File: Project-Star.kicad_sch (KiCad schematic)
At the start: 0 parts

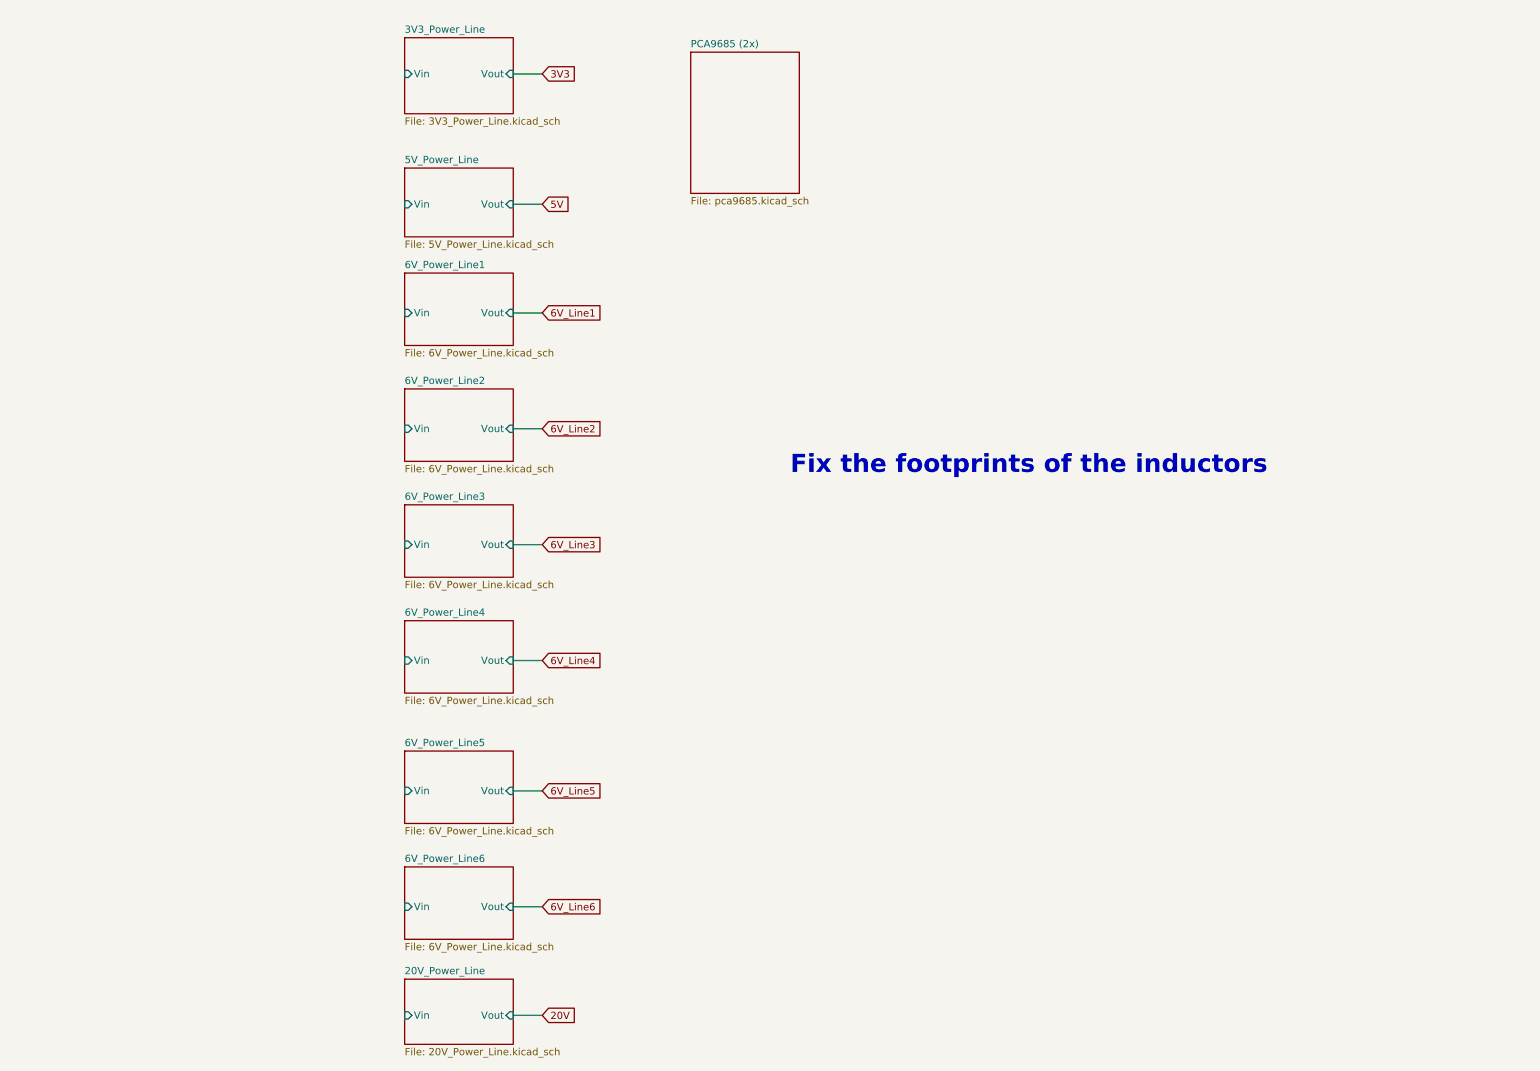
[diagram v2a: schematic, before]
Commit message: 20V line PCB v1
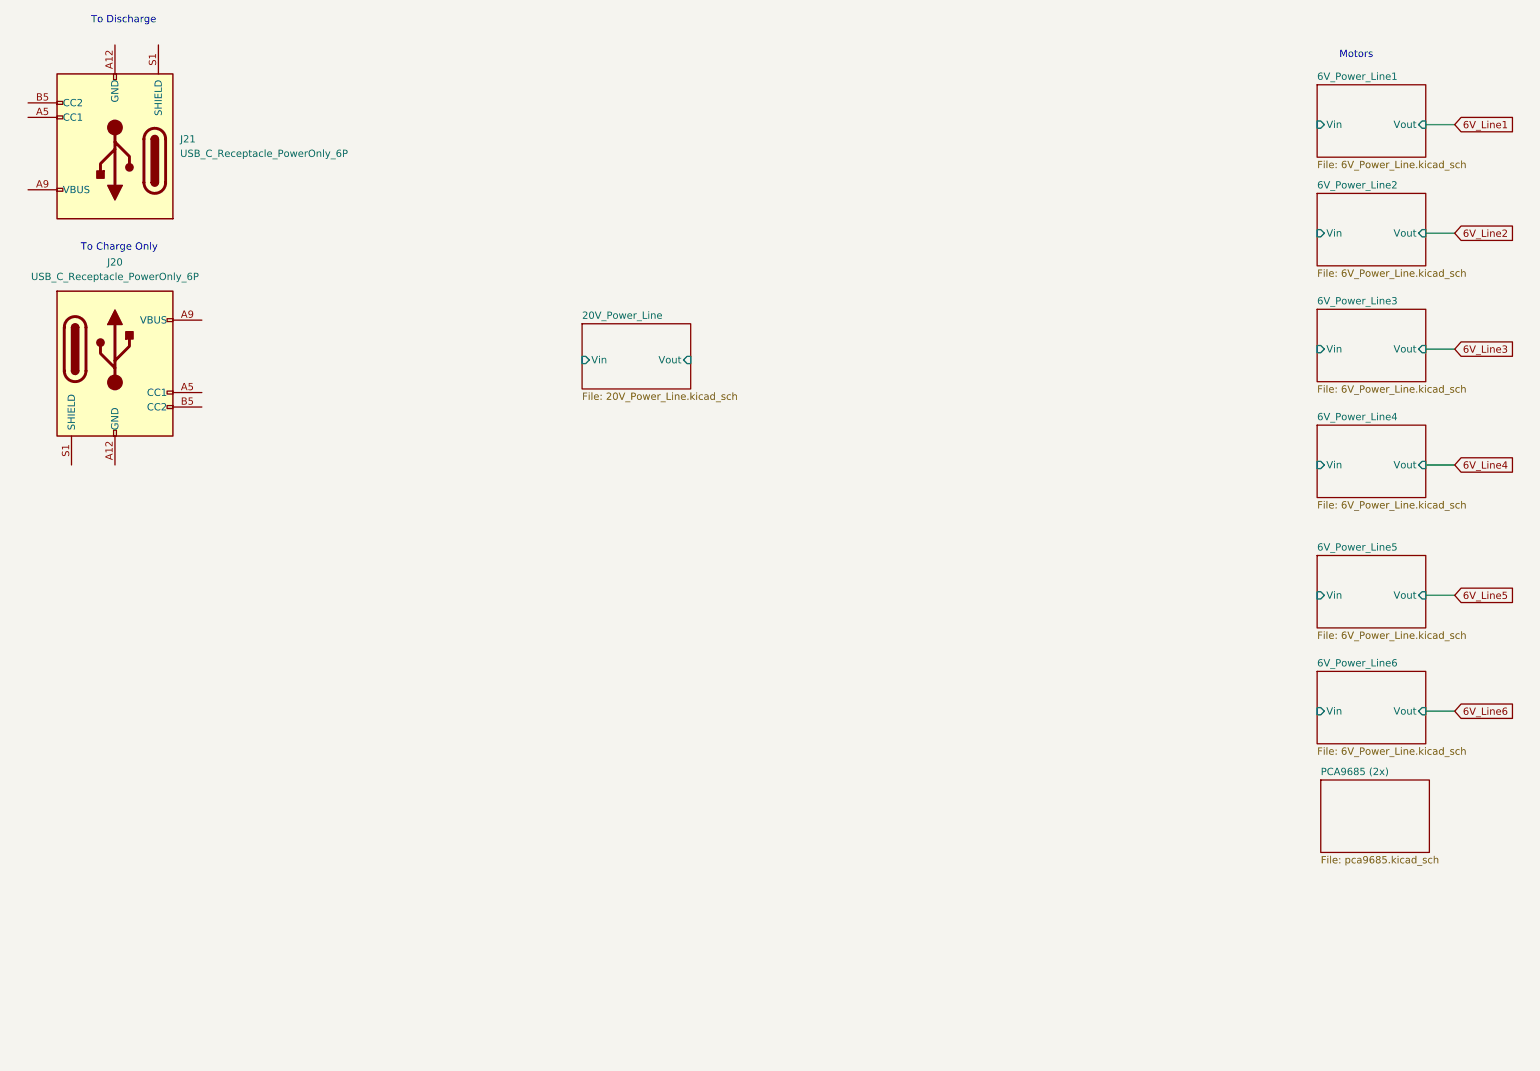
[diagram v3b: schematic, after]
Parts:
- added J20, J21: USB_C_Receptacle_PowerOnly_6P, Connector_USB:USB_C_Receptacle_HRO_TYPE-C-31-M-17, symbol Connector:USB_C_Receptacle_PowerOnly_6P
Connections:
- new net: J21.A12 (GND), J21.B12 (GND)
- new net: J21.A9 (VBUS), J21.B9 (VBUS)
- new net: J20.A12 (GND), J20.B12 (GND)
- new net: J20.A9 (VBUS), J20.B9 (VBUS)
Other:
- removed sheet 3V3_Power_Line
- removed sheet 5V_Power_Line
- note added: "Motors"
- note added: "To Charge Only"
- note added: "To Discharge"
- note removed: "Fix the footprints of the inductors"

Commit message: 20V line V2
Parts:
- renumbered J21 to J1, J20 to J2
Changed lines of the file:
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@@
 		(dnp no)
 		(fields_autoplaced yes)
-		(property "Reference" "J21"
+		(property "Reference" "J1"
 			(at 48.26 35.5599 0)
 			(effects
@@
 			(project "Project-Star"
 				(path "/dfa3d008-01ec-4328-886a-a4a57a49a859"
-					(reference "J21")
+					(reference "J1")
 					(unit 1)
 				)
@@
 		(dnp no)
 		(fields_autoplaced yes)
-		(property "Reference" "J20"
+		(property "Reference" "J2"
 			(at 36.83 57.15 0)
 			(effects
@@
 			(project ""
 				(path "/dfa3d008-01ec-4328-886a-a4a57a49a859"
-					(reference "J20")
+					(reference "J2")
 					(unit 1)
 				)

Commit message: current progress
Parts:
- removed J1, J2: USB_C_Receptacle_PowerOnly_6P, Connector_USB:USB_C_Receptacle_HRO_TYPE-C-31-M-17, symbol Connector:USB_C_Receptacle_PowerOnly_6P
- added C1, C10, C2, C3, C4, C5, C6, C7, C8, C9: 220n, symbol Device:C
- added C11: 4700p, symbol Device:C
- added D1, D2, D3, D4, D5, D6, D7, D8: 5V6, symbol Device:D_Zener_Filled
- added D10, D9: 100V, symbol Device:D_Filled
- added NTC1: 10k, symbol Device:Thermistor
- added Q1, Q2, Q3, Q4, Q5, Q6, Q7, Q8: CSD13380F3, Package_DFN_QFN:Texas_PicoStar_DFN-3_0.69x0.60mm, symbol Transistor_FET:CSD13380F3
- added R1, R11, R16, R19, R24, R26, R6, R8: 10k, symbol Device:R
- added R10, R13, R14, R15, R18, R2, R23, R25, R27, R5, R7: 1k, symbol Device:R
- added R12, R17, R20, R21, R22, R3, R4, R9: 28R7, symbol Device:R
- added R28: 3M, symbol Device:R
- added U1: BQ7693000DBT, Package_SO:TSSOP-30_4.4x7.8mm_P0.5mm, symbol Battery_Management:BQ76930DBT
- added U2: BQ78350DBT-R1, Package_SO:TSSOP-30_4.4x7.8mm_P0.5mm, symbol Battery_Management:BQ78350DBT
- added U3: BQ76200PW, Package_SO:TSSOP-16_4.4x5mm_P0.65mm, symbol Battery_Management:BQ76200PW
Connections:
- new net: D2.1 (K), Q2.1 (G), R6.1
- new net: C2.1, C3.2, R5.2, R6.2, U1.26 (VC1)
- new net: Q6.3 (D), R22.1
- new net: D7.1 (K), Q7.1 (G), R24.1
- new net: Q7.3 (D), R20.1
- new net: D1.1 (K), Q1.1 (G), R1.1
- new net: C1.1, C2.2, R1.2, R2.2, U1.27 (VC0)
- new net: C8.1, D9.2 (A), R23.2, U1.16 (VC10)
- new net: D4.1 (K), Q4.1 (G), R11.1
- new net: Q4.3 (D), R12.1
- new net: D8.1 (K), Q8.1 (G), R26.1
- new net: Q8.3 (D), R21.1
- new net: Q2.3 (D), R4.1
- new net: C8.2, C9.1, R24.2, R25.2, U1.17 (VC9), U1.18 (VC8)
- new net: C4.1, C5.2, R10.2, R11.2, U1.23 (VC4), U1.24 (VC3)
- new net: C10.1, C9.2, R26.2, R27.2, U1.19 (VC7)
- new net: C11.1, NTC1.1, R28.1, U1.13 (TS2)
- new net: C11.2, D10.1 (K), NTC1.2, R28.2, U1.10 (VC5X)
- new net: D6.1 (K), Q6.1 (G), R19.1
- new net: C10.2, C7.1, R18.2, R19.2, U1.20 (VC6)
- new net: C5.1, D10.2 (A), R13.2, U1.22 (VC5)
- new net: U2.22 (VSS), U2.23 (VSS), U2.25 (VSS)
- new net: D3.1 (K), Q3.1 (G), R8.1
- new net: C3.1, C4.2, R7.2, R8.2, U1.25 (VC2)
- new net: C6.1, R15.2, R16.2, U1.21 (VC5B)
- new net: D5.1 (K), Q5.1 (G), R16.1
- new net: D9.1 (K), U1.15 (BAT)
- new net: Q5.3 (D), R17.1
- new net: Q3.3 (D), R9.1
- new net: Q1.3 (D), R3.1
- new net BATT-: D1.2 (A), Q1.2 (S), R2.1
- new net C1: D2.2 (A), Q2.2 (S), R3.2, R5.1
- new net C2: D3.2 (A), Q3.2 (S), R4.2, R7.1
- new net C3: D4.2 (A), Q4.2 (S), R10.1, R9.2
- new net C4: D5.2 (A), Q5.2 (S), R12.2, R13.1, R14.1, R15.1
- new net C5: D6.2 (A), Q6.2 (S), R17.2, R18.1
- new net C6: D8.2 (A), Q8.2 (S), R22.2, R27.1
- new net C7: D7.2 (A), Q7.2 (S), R21.2, R25.1
- new net C8: R20.2, R23.1
- new net GND: C1.2
- new net VCX5: C6.2, C7.2, R14.2
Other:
- removed sheet 20V_Power_Line
- removed sheet 6V_Power_Line1
- removed sheet 6V_Power_Line2
- removed sheet 6V_Power_Line3
- removed sheet 6V_Power_Line4
- removed sheet 6V_Power_Line5
- removed sheet 6V_Power_Line6
- removed sheet PCA9685 (2x)
- note added: "BMC"
- note added: "CHG/DIS"
- note removed: "Motors"
- note removed: "To Charge Only"
- note removed: "To Discharge"

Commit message: v1 design of bms
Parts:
- removed U2: BQ78350DBT-R1, Package_SO:TSSOP-30_4.4x7.8mm_P0.5mm, symbol Battery_Management:BQ78350DBT
- added C12, C19, C20, C22, C24, C25, C26, C32: 1u, symbol Device:C
- added C13, C14, C27, C28, C33, C36: 100n, symbol Device:C
- added C15, C37: 4u7, symbol Device:C
- added C16: 370p, symbol Device:C
- added C17, C18: 10u, symbol Device:C
- added C21: 4700p, symbol Device:C
- added C23: 470p, symbol Device:C
- added C29: 1.5u, symbol Device:C
- added C30, C31: 1n, symbol Device:C
- added C34: 2200p, symbol Device:C
- added D11, D13: 100V, symbol Device:D_Filled
- added D12: 200V, symbol Device:D_Filled
- added D14, D15, D16: 3V9, symbol Device:D_Zener_Filled
- added D17, D18: 16V, symbol Device:D_Zener_Filled
- added D19: 18V, symbol Device:D_Zener_Filled
- added D20, D21, D22, D23: GREEN, LED_THT:LED_D5.0mm, symbol PCM_SL_Devices:LED
- added D24, D25, D26, D27, D28, D29: 5V6, symbol Device:D_Zener_Filled
- added F2: 50V, 30A, Slow Blow, symbol PCM_Device_AKL:Fuse
- added FB1, FB2, FB3, FB4: 200R, symbol Device:FerriteBead
- added J1: Conn_01x02, 4ms_Connector:Pins_1x02_2.54mm_TH, symbol PCM_4ms_Connector:Conn_01x02
- added J2: Conn_02x04, 4ms_Connector:Pins_2x04_2.54mm_TH, symbol PCM_4ms_Connector:Conn_02x04
- added J3: Conn_01x09, 4ms_Connector:Pins_1x09_2.54mm_TH, symbol PCM_4ms_Connector:Conn_01x09
- added J4: Screw_Terminal_01x02, symbol Connector:Screw_Terminal_01x02
- added NT1, NT2, NT3: NetTie, symbol Device:NetTie_2
- added NTC2: 10k, symbol Device:Thermistor
- added Q10, Q11, Q14, Q15, Q16, Q17: Q_NMOS, symbol Device:Q_NMOS
- added Q12, Q13, Q19: Q_PMOS, symbol Device:Q_PMOS
- added Q18: Q_NPN, symbol Device:Q_NPN
- added Q20: TP0610K, PCM_Package_TO_SOT_SMD_AKL:SOT-23, symbol PCM_Transistor_MOSFET_AKL:TP0610K
- added Q21, Q9: 2N7002E, PCM_Package_TO_SOT_SMD_AKL:SOT-23, symbol PCM_Transistor_MOSFET_AKL:2N7002E
- added R29, R30, R65, R73, R74, R90: 10k, symbol Device:R
- added R31: 510k, symbol Device:R
- added R32, R34, R42, R87, R88, R91: 100k, symbol Device:R
- added R33, R46, R47, R58, R59, R61, R75, R76, R77, R78, R79, R80, R81, R82, R83, R84, R85, R86: 100R, symbol Device:R
- added R35, R37, R38, R64, R67, R68, R69, R70, R71: 1k, symbol Device:R
- added R36: 3M, symbol Device:R
- added R39: 51k, symbol Device:R
- added R40, R43, R52, R53, R54: 10M, symbol Device:R
- added R41: 1M, symbol Device:R
- added R44, R45, R60, R63: 0R, symbol Device:R
- added R48, R49, R50, R51: 1k2, symbol Device:R
- added R55, R56, R57: 620R, symbol Device:R
- added R62: 750, symbol Device:R
- added R66: 154k, symbol Device:R
- added R72: 3k, symbol Device:R
- added R89: 130k, symbol Device:R
- added SW1: SW_Push, symbol Switch:SW_Push
- added TVS1: SMAJ40A, Diode_SMD:D_SMA, symbol Diode:SMAJ40A
- added TVS2, TVS3: 5.0SMDJ36A, Diode_SMD:D_SMC, symbol Diode:Z3SMCxxx
- added U2: TPS3839DBZ, Package_TO_SOT_SMD:SOT-23, symbol Power_Supervisor:TPS3839DBZ
- added U4: LMT01LPG, Package_TO_SOT_THT:TO-92-2, symbol Sensor_Temperature:LMT01LPG
- added U5: MSP430G2553IPW20, Package_SO:TSSOP-20_4.4x6.5mm_P0.65mm, symbol MCU_Texas_MSP430:MSP430G2553IPW20
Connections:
- net C1: now also J3.2 (Pin_2)
- net C2: now also J3.3 (Pin_3)
- net C3: now also J3.4 (Pin_4)
- net C4: now also J3.5 (Pin_5)
- net C5: now also J3.6 (Pin_6)
- net C6: now also J3.7 (Pin_7)
- net C7: now also J3.8 (Pin_8)
- net GND: now also U1.3 (VSS), U3.9 (VSS), C15.2, C16.2, C17.1, C19.1, C20.1, C21.2, C22.2, C24.2, C26.1, C30.1, C31.1, C32.2, C33.2, C34.2, C36.2, C37.2, D14.2 (A), D15.2 (A), D24.2 (A), D25.2 (A), D26.2 (A), D27.2 (A), D28.2 (A), D29.2 (A), J2.4 (Pin_4), J2.5 (Pin_5), J2.6 (Pin_6), NT1.1, NTC2.2, Q11.S, Q21.2 (S), R31.2, R36.2, R40.1, R65.1, R68.1, R69.1, R70.1, R71.1, R73.2, R90.1, R91.1, SW1.1, TVS1.2 (A2), U2.1 (GND), U5.20 (DVSS)
- net VCX5: now also C11.2, D10.1 (K), D9.1 (K), NTC1.2, R28.2, U1.10 (VC5X), U1.15 (BAT), C12.2, C17.2, C18.1, C18.2, R32.2, R35.2
- net at C8.1, D9.2 (A), R23.2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: now also TVS1.1 (A1)
- net VDDCP: now reaches U3.1 (VDDCP)
- net VDDCP: now also C29.2
- net PACKDIV: now reaches U3.10 (PACKDIV)
- net PACK: now reaches U3.11 (PACK)
- net PACK: now also R60.2, R61.1, R89.1, R90.2, U5.6 (TCK/SMCLK/UCB0STE/UCA0CLK/VREF+/VeREF+/CA4/A4/P1.4)
- net DSG: now reaches U3.12 (DSG)
- net DSG: now also D19.1 (K), R57.2
- net BAT: now reaches U3.2 (BAT)
- net BAT: now also C29.1, C30.2, R58.2
- net CHG_EN: now reaches U3.4 (CHG_EN)
- net CHG_EN: now also U1.2 (CHG)
- net CP_EN: now reaches U3.5 (CP_EN)
- net DSG_EN: now reaches U3.6 (DSG_EN)
- net DSG_EN: now also U1.1 (DSG)
- net PMON_EN: now reaches U3.7 (PMON_EN)
- net PCHG_EN: now reaches U3.8 (PCHG_EN)
- net at U1.11 (NC(CAP2)): now also U1.12 (NC(CAP2)), U1.14 (CAP2), C12.1
- net at U1.28 (SRP): now also C24.1, C25.2, R46.2
- net ISENSE: now reaches U1.29 (SRN)
- net ISENSE: now also C25.1, C26.2, R47.2, R67.2
- net ALERT: now reaches U1.30 (ALERT)
- net ALERT: now also C16.1, R31.1, U5.2 (TA0CLK/ACLK/CA0/A0/P1.0)
- net SDA: now reaches U1.4 (SDA)
- net SDA: now also R29.1, R76.2, U5.15 (TDO/TDI/UCB0SIMO/UCB0SDA/CAOUT/CA7/A7/P1.7)
- net SCL: now reaches U1.5 (SCL)
- net SCL: now also R30.1, R75.2, U5.14 (TDI/TCLK/UCB0SOMI/UCB0SCL/TA0.1/CA6/A6/P1.6)
- net TS1: now reaches U1.6 (TS1)
- net TS1: now also C21.1, D13.1 (K), NTC2.1, R36.1
- net at U1.7 (CAP1): now also C22.1, Q18.B
- net REGOUT: now reaches U1.8 (REGOUT)
- net REGOUT: now also C15.1, C33.1, C36.1, C37.1, J2.3 (Pin_3), Q19.D, R29.2, R30.2, R42.2, R74.2, U2.3 (VDD), U5.1 (DVCC)
- net REGSRC: now reaches U1.9 (REGSRC)
- net REGSRC: now also C19.2, Q9.2 (S)
- net BATT- renamed -BATT
- net -BATT: now also J3.1 (Pin_1), J4.2 (Pin_2), NT1.2, NT2.1, R44.1, R45.1, R63.1, TVS2.2 (A)
- net C8 renamed +BATT
- net +BATT: now also C23.2, D11.2 (A), F2.1, J3.9 (Pin_9), J4.1 (Pin_1), Q20.3 (D), R34.2, R35.1, R62.2, R87.2, TVS2.1 (K)
- new net: D13.2 (A), D14.1 (K), R37.1, R39.1
- new net: R64.2, R65.2, R66.1, R67.1
- new net: Q9.1 (G), R32.1
- new net: FB1.2, Q14.G
- new net: Q10.G, Q11.D, R40.2, R41.1
- new net: Q10.D, Q12.D, R41.2
- new net: D25.1 (K), R76.1, R77.2
- new net: D22.1, R70.2
- new net: D22.2, U5.11 (P2.3/TA1.0)
- new net: D27.1 (K), R81.1, R82.2
- new net: D28.1 (K), R83.1, R84.2
- new net: D20.1, R68.2
- new net: D20.2, U5.9 (P2.1/TA1.1)
- new net: Q20.1 (G), R87.1, R88.2
- new net: Q20.2 (S), R89.2
- new net: R64.1, U5.5 (CAOUT/VREF-/VeREF-/CA3/A3/P1.3)
- new net: D23.1, R71.2
- new net: D23.2, U5.12 (P2.4/TA1.2)
- new net: D21.1, R69.2
- new net: Q21.1 (G), R91.2
- new net: Q21.3 (D), R88.1
- new net: C20.2, Q9.3 (D), R33.1
- new net: J1.1 (Pin_1), R77.1
- new net: C31.2, R59.2, R60.1
- new net: Q16.D, Q17.D
- new net: FB3.2, Q17.G
- new net: FB4.2, Q15.G
- new net: C23.1, D16.2 (A), Q12.G, R43.1
- new net: Q11.G, R42.1
- new net: C27.1, D17.2 (A), F2.2, Q14.S, Q16.S, R48.1, R49.1, R50.1, R51.1, R53.1, R58.1
- new net: Q13.G, R52.1
- new net: R72.1, SW1.2
- new net: D19.2 (A), R61.2
- new net: D15.1 (K), R37.2, R38.1
- new net: Q19.S, R66.2
- new net: D24.1 (K), R75.1, R78.2
- new net: U2.2 (~{RESET}), U5.18 (P2.7/XOUT)
- new net: C13.2, C14.1
- new net: Q10.S, R39.2
- new net: D26.1 (K), R79.1, R80.2
- new net: D29.1 (K), R85.1, R86.2
- new net: D21.2, U5.10 (P2.2/TA1.1)
- new net: R72.2, U5.13 (P2.5/TA1.2)
- new net: Q19.G, U5.19 (P2.6/XIN/TA0.1)
- new net: U4.2 (VP), U5.8 (P2.0/TA1.0)
- new net: C27.2, C28.1
- new net: D11.1 (K), R33.2, R34.1
- new net: J1.2 (Pin_2), R78.1
- new net: Q18.C, R62.1
- new net: FB2.2, Q16.G
- new net CD: Q13.S, Q14.D, Q15.D, R52.2, R55.1
- new net CGATE: D17.1 (K), FB1.1, FB2.1, R53.2, R56.1
- new net CHG: R56.2
- new net DGATE: D18.1 (K), FB3.1, FB4.1, R54.2, R57.1
- new net J_SBTWDIO: J2.1 (Pin_1), R86.1
- new net J_SBTWTCK: J2.2 (Pin_2), R84.1
- new net J_UCA0RXD: J2.8 (Pin_8), R82.1
- new net J_UCA0TXD: J2.7 (Pin_7), R80.1
- new net LEDP: C32.1, Q18.E
- new net PACK+: C13.1, C28.2, D12.1 (K), D16.1 (K), D18.2 (A), Q12.S, Q15.S, Q17.S, R43.2, R54.1, R59.1, TVS3.1 (K)
- new net PACK-: C14.2, D12.2 (A), NT3.1, R44.2, R45.2, R63.2, TVS3.2 (A)
- new net PCHG: R55.2
- new net PDRAIN: Q13.D, R48.2, R49.2, R50.2, R51.2
- new net SBTWDIO: C34.1, R74.1, R85.2, U5.16 (~{RST}/NMI/SBWTDIO)
- new net SBTWTCK: R83.2, U5.17 (TEST/SBWTCK)
- new net SNSN: NT3.2, R47.1
- new net SNSP: NT2.2, R46.1
- new net TMP: R73.1, U4.1 (VN), U5.7 (TMS/UCB0CLK/UCA0STE/TA0.0/CA5/A5/P1.5)
- new net UCA0RXD: R81.2, U5.3 (UCA0RXD/UCA0SOMI/TA0.0/CA1/A1/P1.1)
- new net UCA0TXD: R79.2, U5.4 (UCA0TXD/UCA0SIMO/TA0.1/CA2/A2/P1.2)
- new net WAKE: R38.2
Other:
- note removed: "BMC"
- note removed: "CHG/DIS"
- moved on the sheet: C1, C10, C11, C2, C3, C4, C5, C6, C7, C8, C9, D1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
